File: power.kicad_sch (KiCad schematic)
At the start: 29 parts, among them U11 AP2114H-3.3TRG1, U5 INA226, U7 TPS54560DDAR, U9 TPS7A2033DQNR

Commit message: corrections and IO updated
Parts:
- added C32: 100uF, Capacitor_SMD:C_0201_0603Metric_Pad0.64x0.40mm_HandSolder, symbol Device:C_Small
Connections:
- net GND: now also C32.2
- net VBAT: now also C32.1
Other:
- moved on the sheet: C21, C22, C23, C24, C25, C26, C27, C28, C29, C30, C31, C34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

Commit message: mcu updates
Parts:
- removed C37: 4.7uF, Capacitor_SMD:C_0201_0603Metric_Pad0.64x0.40mm_HandSolder, symbol Device:C_Small
- added C42, C44: 10uF, Capacitor_SMD:C_0201_0603Metric_Pad0.64x0.40mm_HandSolder, symbol Device:C_Small
- added C45: 4.7uF, Capacitor_SMD:C_0201_0603Metric_Pad0.64x0.40mm_HandSolder, symbol Device:C_Small
- C36: value 1uF -> 4.7uF
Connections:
- net +3V3: now also C38.1, U11.2 (VOUT)
- net 5V: now also C42.1
- net GND: now also C38.2, C42.2, C44.2, C45.2; no longer C38.1
- net Vin_3.3: now reaches U11.3 (VIN)
- net Vin_3.3: now also C44.1, C45.1; no longer C38.2
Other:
- moved on the sheet: C35

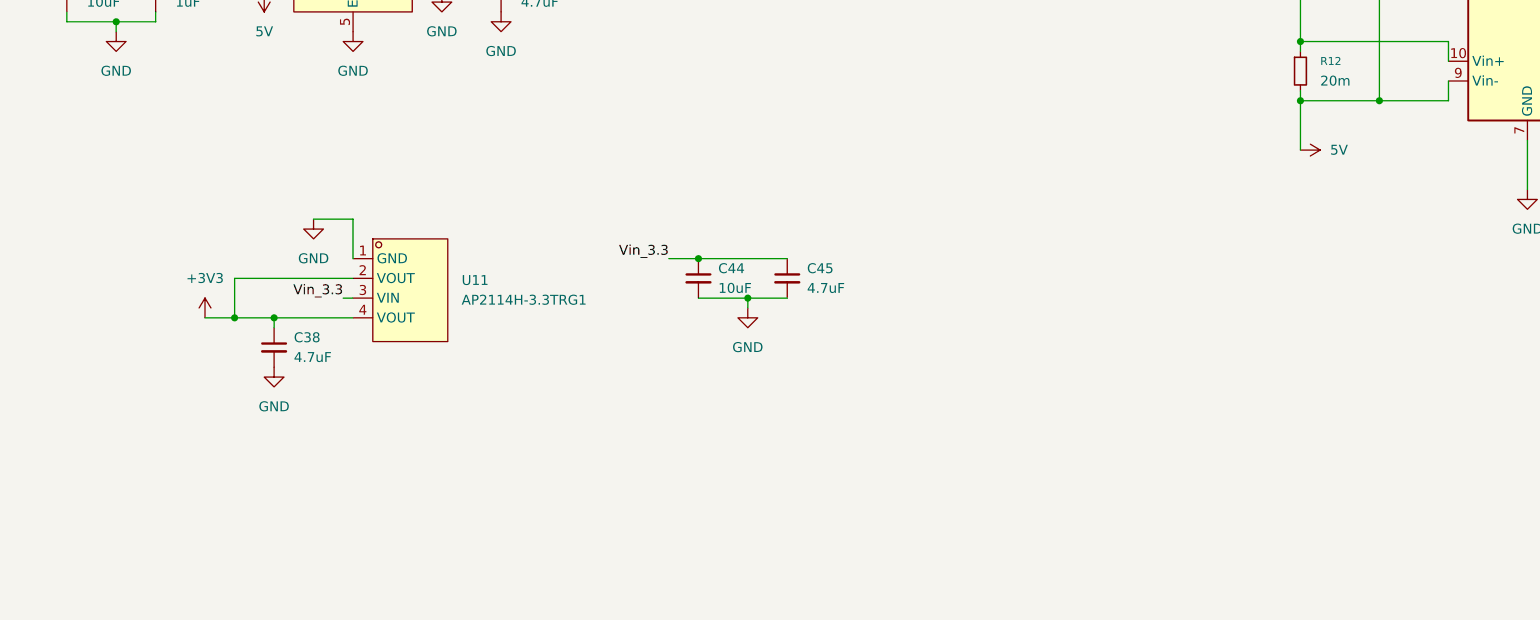
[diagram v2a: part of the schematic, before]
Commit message: added in RF componentys and updated and reviewed STM connections
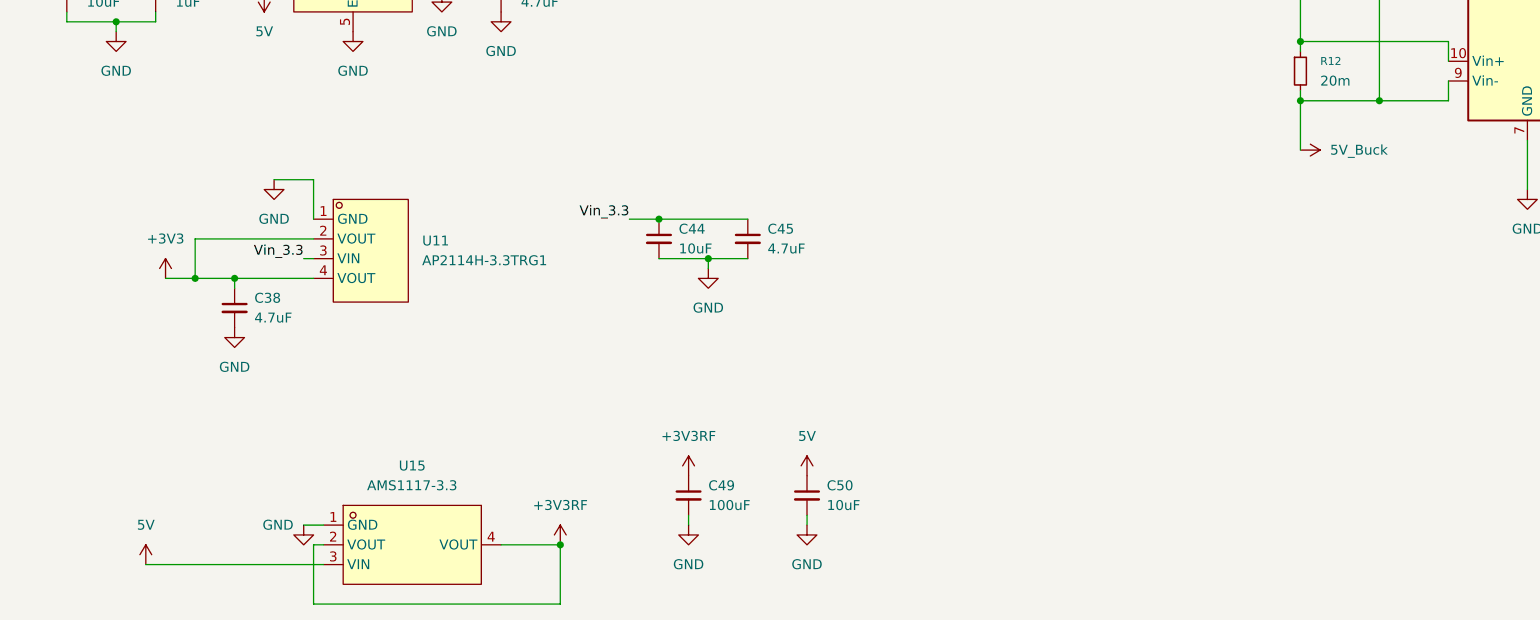
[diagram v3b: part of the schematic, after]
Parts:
- added C49: 100uF, Capacitor_SMD:C_0201_0603Metric_Pad0.64x0.40mm_HandSolder, symbol Device:C_Small
- added C50: 10uF, Capacitor_SMD:C_0201_0603Metric_Pad0.64x0.40mm_HandSolder, symbol Device:C_Small
- added U15: AMS1117-3.3, LCSC:SOT-223-3_L6.5-W3.4-P2.30-LS7.0-BR, symbol LCSC:AMS1117-3.3
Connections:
- net 5V: now also C50.1, U15.3 (VIN); no longer R12.2, U5.8 (Vbus), U5.9 (Vin-)
- net GND: now also C49.2, C50.2, U15.1 (GND)
- new net +3V3RF: C49.1, U15.2 (VOUT), U15.4 (VOUT)
- new net 5V_Buck: R12.2, U5.8 (Vbus), U5.9 (Vin-)
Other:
- moved on the sheet: C38, C44, C45, U11

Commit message: finalized RF
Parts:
- added JP6: Jumper_2_Open, symbol Jumper:Jumper_2_Open
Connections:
- net +3V3RF: now also JP6.2 (B); no longer U15.2 (VOUT), U15.4 (VOUT)
- new net: JP6.1 (A), U15.2 (VOUT), U15.4 (VOUT)
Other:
- moved on the sheet: C35, C36, C38, C42, C44, C45, C49, C50, U11, U15, U9
